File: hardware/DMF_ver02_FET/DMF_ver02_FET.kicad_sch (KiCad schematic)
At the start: 44 parts, among them J1 GND_Electrodes, J10 GND, J2 POWER, J3 GND_Electrodes, J4 Ard_1, J5 Ard_2, J6 Ard_3, J7 Ard_4, J8 Ard_5, J9 Ard_6, Q1 IRF740, Q2 IRF740, Q3 IRF740, Q4 IRF740, Q5 IRF740, Q6 IRF740

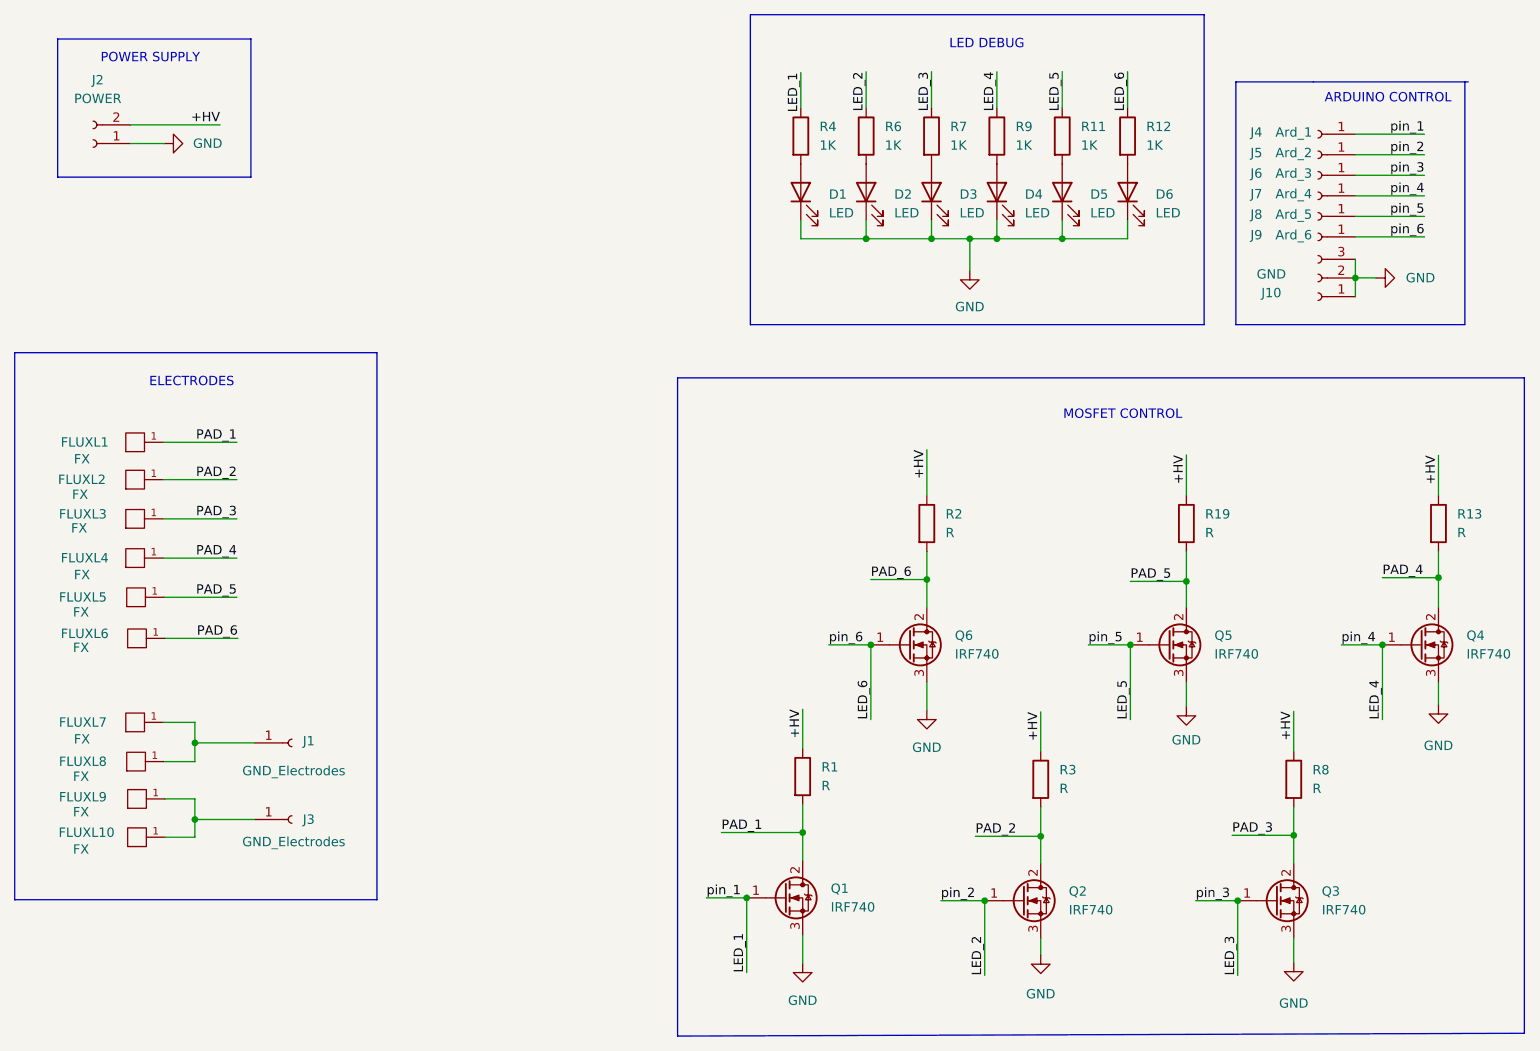
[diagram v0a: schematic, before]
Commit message: Create DMF board version SMD
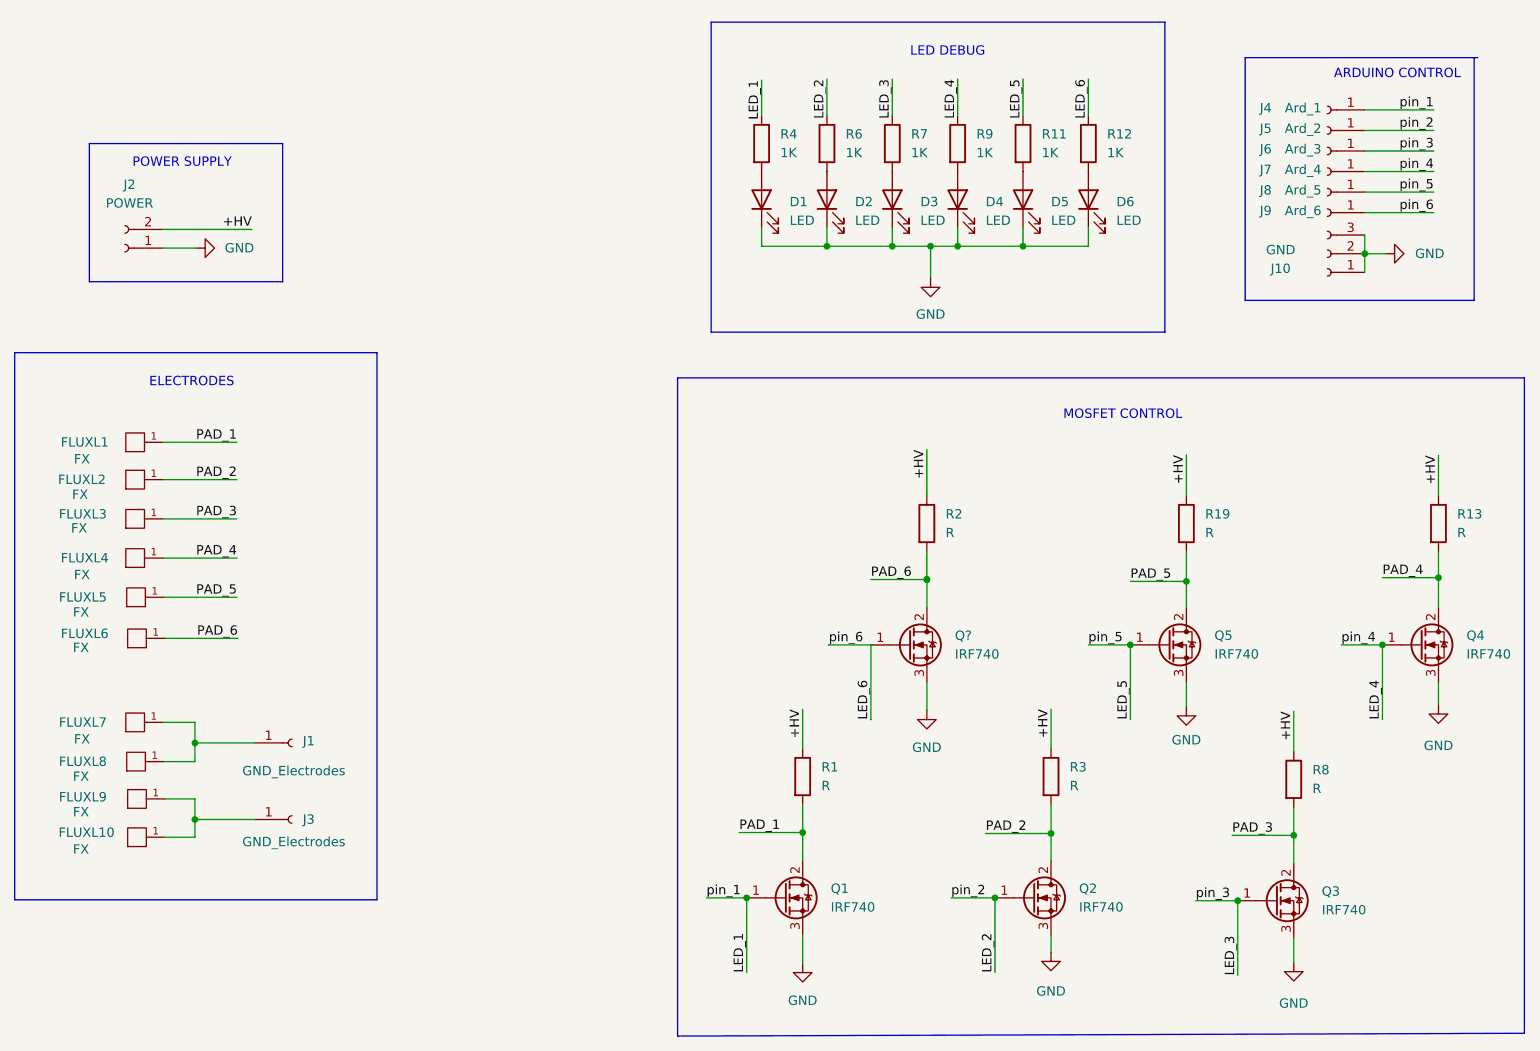
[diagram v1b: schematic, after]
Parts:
- removed Q6: IRF740, Package_TO_SOT_THT:TO-220-3_Vertical, symbol Transistor_FET:IRF740
- added Q?: IRF740, Package_TO_SOT_SMD:TO-263-3_TabPin2, symbol Transistor_FET:IRF740
- D1, D2, D3, D4, D5, D6: footprint LED_THT:LED_D5.0mm_IRBlack -> LED_SMD:LED_0603_1608Metric_Pad1.05x0.95mm_HandSolder
- Q1, Q2, Q3, Q4, Q5: footprint Package_TO_SOT_THT:TO-220-3_Vertical -> Package_TO_SOT_SMD:TO-263-3_TabPin2
- R1, R11, R12, R13, R19, R2, R3, R4, R6, R7, R8, R9: footprint Resistor_THT:R_Axial_DIN0207_L6.3mm_D2.5mm_P10.16mm_Horizontal -> Resistor_SMD:R_1206_3216Metric_Pad1.30x1.75mm_HandSolder
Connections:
- net GND: now also Q?.3 (S)
- net LED_6: now also Q?.1 (G)
- net PAD_6: now also Q?.2 (D)
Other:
- moved on the sheet: D1, D2, D3, D4, D5, D6, J10, J2, J4, J5, J6, J7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

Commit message: Update PCB layout: Placed components.
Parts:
- removed J10: GND, Connector_PinSocket_2.54mm:PinSocket_1x03_P2.54mm_Vertical, symbol Connector:Conn_01x03_Female
- removed J4: Ard_1, Connector_PinSocket_2.54mm:PinSocket_1x01_P2.54mm_Vertical, symbol Connector:Conn_01x01_Female
- removed J5: Ard_2, Connector_PinSocket_2.54mm:PinSocket_1x01_P2.54mm_Vertical, symbol Connector:Conn_01x01_Female
- removed J6: Ard_3, Connector_PinSocket_2.54mm:PinSocket_1x01_P2.54mm_Vertical, symbol Connector:Conn_01x01_Female
- removed J7: Ard_4, Connector_PinSocket_2.54mm:PinSocket_1x01_P2.54mm_Vertical, symbol Connector:Conn_01x01_Female
- removed J8: Ard_5, Connector_PinSocket_2.54mm:PinSocket_1x01_P2.54mm_Vertical, symbol Connector:Conn_01x01_Female
- removed J9: Ard_6, Connector_PinSocket_2.54mm:PinSocket_1x01_P2.54mm_Vertical, symbol Connector:Conn_01x01_Female
- added J4: Conn_01x09_Female, Connector_PinHeader_2.54mm:PinHeader_1x09_P2.54mm_Vertical, symbol Connector:Conn_01x09_Female
- gave numbers to parts that had none: 1
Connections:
- net GND: now also J4.1 (Pin_1), J4.2 (Pin_2), J4.3 (Pin_3)
- net LED_1: now also J4.9 (Pin_9)
- net LED_2: now also J4.8 (Pin_8)
- net LED_3: now also J4.7 (Pin_7)
- net LED_4: now also J4.6 (Pin_6)
- net LED_5: now also J4.5 (Pin_5)
- net LED_6: now also J4.4 (Pin_4)
